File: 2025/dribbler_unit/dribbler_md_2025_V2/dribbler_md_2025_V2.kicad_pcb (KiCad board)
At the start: 2 copper layers, 82 x 23 mm, 87 parts, among them J1 Conn_01x02_Pin, J2 Conn_01x04_Pin, J3 Conn_01x05_Pin, J4 Conn_01x07_Pin, SW1 SW_Wuerth_450301014042, SW2 SW_MEC_5E, SW3 SW_Wuerth_450301014042, SW4 SW_MEC_5E, U1 MAX3051, U2 STS8DN3LLH5, U3 STS8DN3LLH5, U4 DRV8701, U5 STM32F446RETx, Y1 Crystal_GND2

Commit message: 抵抗を追加
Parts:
- added R30: 0, Resistor_SMD:R_0603_1608Metric_Pad0.98x0.95mm_HandSolder, B.Cu at (226.7, 86.2)
- added R31: 0, Resistor_SMD:R_0603_1608Metric_Pad0.98x0.95mm_HandSolder, B.Cu at (226.7, 87.7)
- REG1: value AP7333 -> MCP1703AT-3302E/CB
- moved R19 0.13 mm to (226.7, 83.1)
- moved R20 0.13 mm to (226.7, 84.7)
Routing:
- net GND_main: vias 25 -> 29
- net GND_log: vias 53 -> 54

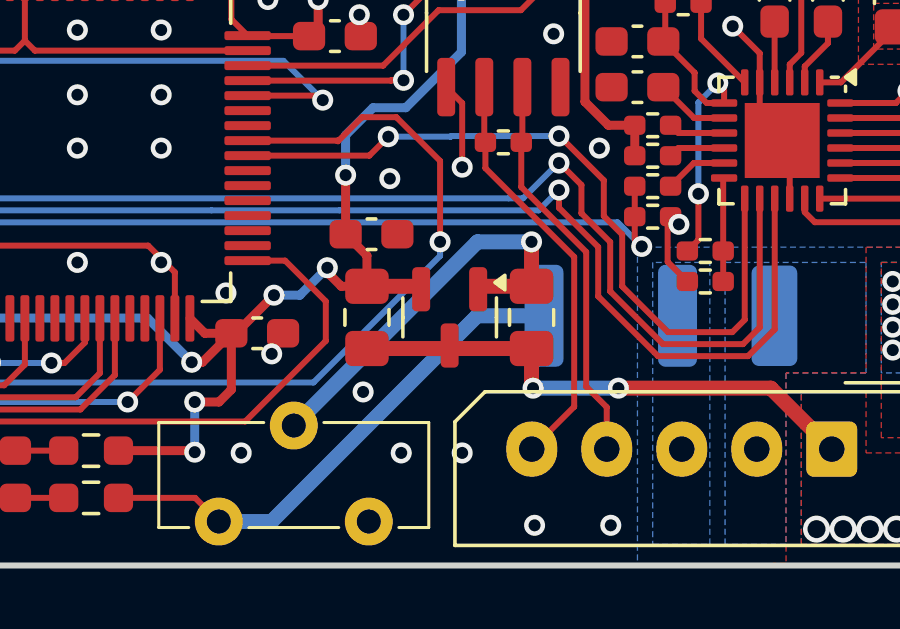
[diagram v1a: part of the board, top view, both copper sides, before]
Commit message: 三端子レギュレータのフットプリント変更
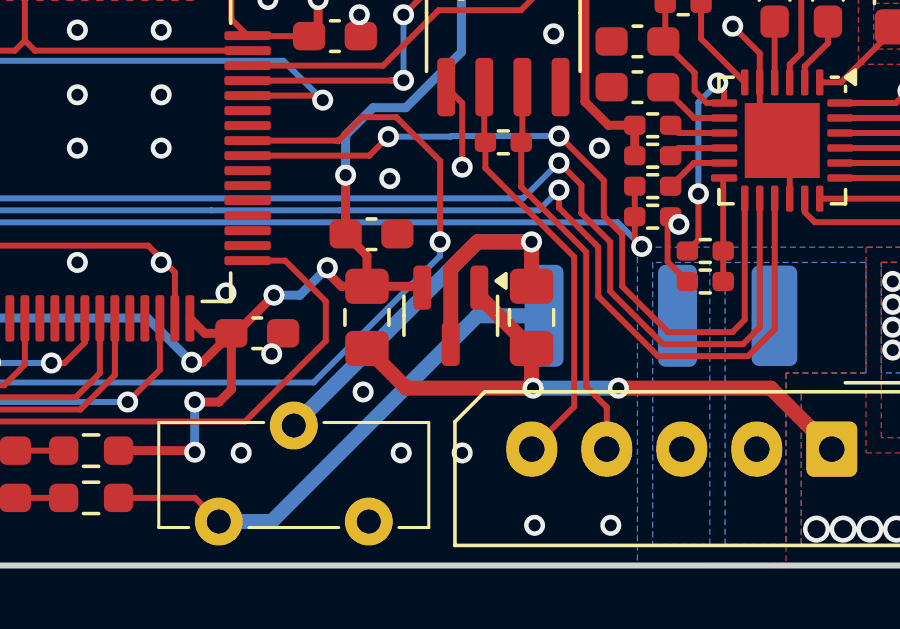
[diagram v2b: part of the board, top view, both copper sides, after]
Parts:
- moved REG1 0.07 mm to (208.5, 96.5)
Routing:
- net Net-(REG1-VIN): track 13.8 -> 17.5 mm
- net GND_main: track 31.0 -> 34.3 mm
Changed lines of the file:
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@@
 	(footprint "Package_TO_SOT_SMD:SOT-23"
 		(layer "F.Cu")
-		(at 208.5073 96.5297 -90)
+		(at 208.544 96.475 -90)
 		(descr "SOT, 3 Pin (https://www.jedec.org/system/files/docs/to-236h.pdf variant AB), generated with kicad-footprint-generator ipc_gullwing_generator.py")
 		(tags "SOT TO_SOT_SMD")
@@
 		)
 		(pad "1" smd roundrect
-			(at -0.9375 -0.95 270)
+			(at 0.9375 0 270)
 			(size 1.475 0.6)
 			(layers "F.Cu" "F.Paste" "F.Mask")
@@
 		)
 		(pad "3" smd roundrect
-			(at 0.9375 0 270)
+			(at -0.9375 -0.95 270)
 			(size 1.475 0.6)
 			(layers "F.Cu" "F.Paste" "F.Mask")
@@
 	)
 	(segment
-		(start 205.75 95.4922)
-		(end 207.4573 95.4922)
-		(width 0.5)
+		(start 207.5487 95.4922)
+		(end 207.594 95.5375)
+		(width 0.3)
 		(layer "F.Cu")
 		(net 1)
@@
 	)
 	(segment
-		(start 207.4573 95.4922)
-		(end 207.5573 95.5922)
-		(width 0.5)
-		(layer "F.Cu")
-		(net 1)
-	)
-	(segment
 		(start 200.0096 99.3492)
 		(end 200.8184 99.3492)
@@
 	)
 	(segment
+		(start 205.75 95.4922)
+		(end 207.5487 95.4922)
+		(width 0.3)
+		(layer "F.Cu")
+		(net 1)
+	)
+	(segment
 		(start 213.878 83.4967)
 		(end 213.017 84.3577)
@@
 	)
 	(segment
+		(start 207.0708 98.888)
+		(end 211.2872 98.888)
+		(width 0.5)
+		(layer "F.Cu")
+		(net 3)
+	)
+	(segment
 		(start 211.2364 97.5672)
 		(end 211.2364 98.8372)
@@
 	)
 	(segment
-		(start 205.75 97.5672)
-		(end 211.2364 97.5672)
+		(start 209.494 95.5375)
+		(end 209.494 95.8248)
 		(width 0.5)
 		(layer "F.Cu")
@@
 	)
 	(segment
+		(start 209.494 95.8248)
+		(end 211.2364 97.5672)
+		(width 0.5)
+		(layer "F.Cu")
+		(net 3)
+	)
+	(segment
+		(start 205.75 97.5672)
+		(end 207.0708 98.888)
+		(width 0.5)
+		(layer "F.Cu")
+		(net 3)
+	)
+	(segment
 		(start 214.132 98.888)
 		(end 219.212 98.888)
@@
 	)
 	(segment
+		(start 208.544 94.897316)
+		(end 209.430116 94.0112)
+		(width 0.5)
+		(layer "F.Cu")
+		(net 10)
+	)
+	(segment
 		(start 211.2364 95.4922)
 		(end 211.2364 94.0112)
@@
 	)
 	(segment
-		(start 209.5573 95.4922)
-		(end 209.4573 95.5922)
+		(start 209.430116 94.0112)
+		(end 211.2364 94.0112)
 		(width 0.5)
 		(layer "F.Cu")
@@
 	)
 	(segment
-		(start 211.2364 95.4922)
-		(end 209.5573 95.4922)
+		(start 208.544 97.4125)
+		(end 208.544 94.897316)
 		(width 0.5)
 		(layer "F.Cu")
